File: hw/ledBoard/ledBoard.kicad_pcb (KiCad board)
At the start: 4 copper layers, 34.2 x 34.3 mm, 35 parts, among them J1 Conn_01x13_Socket, J2 Conn_01x13_Socket, J6 726386-2, J7 726386-2, Q1 NMOS, Q2 NMOS, U4 LM5148RGYR

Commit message: hw - ledBoard
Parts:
- removed C21: 470nF, Capacitor_SMD:C_0805_2012Metric_Pad1.18x1.45mm_HandSolder
- removed C22, C23: 100nF, Capacitor_SMD:C_0805_2012Metric_Pad1.18x1.45mm_HandSolder
- removed C24: 4.7uF, Capacitor_SMD:C_0805_2012Metric_Pad1.18x1.45mm_HandSolder
- removed C25: 22p, Capacitor_SMD:C_0805_2012Metric_Pad1.18x1.45mm_HandSolder
- removed C26: 10uF, Capacitor_SMD:C_1210_3225Metric_Pad1.33x2.70mm_HandSolder
- removed C27: 2.7nF, Capacitor_SMD:C_0805_2012Metric_Pad1.18x1.45mm_HandSolder
- removed J7: 726386-2, FASTON:726386-2
- removed NT2: NetTie_2, NetTie:NetTie-2_SMD_Pad0.5mm
- removed Q1, Q2: NMOS, NMOS-CSD18514:DQJ0008A
- removed Rt1: 35.7k, Resistor_SMD:R_0805_2012Metric_Pad1.20x1.40mm_HandSolder
- removed U4: LM5148RGYR, LM5148:VQFN24_RGY_TEX
- added C1: 470nF, Capacitor_SMD:C_0805_2012Metric_Pad1.18x1.45mm_HandSolder, F.Cu at (206.6, 85.8)
- added C19: 0.01uF, Capacitor_SMD:C_0805_2012Metric_Pad1.18x1.45mm_HandSolder, F.Cu at (227.3, 78.4)
- added C2: 10uF, Capacitor_SMD:C_1210_3225Metric_Pad1.33x2.70mm_HandSolder, F.Cu at (214.5, 94.3)
- added C20: 0.01uF, Capacitor_SMD:C_0805_2012Metric_Pad1.18x1.45mm_HandSolder, F.Cu at (228.2, 74.5)
- added C3: 10uF, Capacitor_SMD:C_1210_3225Metric_Pad1.33x2.70mm_HandSolder, F.Cu at (214.5, 91.0)
- added C4: 0.01uF, Capacitor_SMD:C_0805_2012Metric_Pad1.18x1.45mm_HandSolder, F.Cu at (220.9, 90.9)
- added C5: 0.01uF, Capacitor_SMD:C_0805_2012Metric_Pad1.18x1.45mm_HandSolder, F.Cu at (220.9, 95.0)
- added C6: C, Capacitor_SMD:C_0805_2012Metric_Pad1.18x1.45mm_HandSolder, F.Cu at (201.4, 89.3)
- added C7: C, Capacitor_SMD:C_0805_2012Metric_Pad1.18x1.45mm_HandSolder, F.Cu at (204.5, 88.4)
- added C8: 47uF, Capacitor_SMD:C_1210_3225Metric_Pad1.33x2.70mm_HandSolder, B.Cu at (224.2, 83.4)
- added C9: 47uF, Capacitor_SMD:C_1210_3225Metric_Pad1.33x2.70mm_HandSolder, B.Cu at (219.1, 83.4)
- added D2: D, Diode_SMD:D_SOD-523, F.Cu at (200.7, 92.3)
- added D3: STPS3L40UF, STPS3L40:SODFL5436X110N, F.Cu at (211.5, 84.6)
- added D4: D, Diode_SMD:D_SOD-523, B.Cu at (203.1, 81.2)
- added G***: LOGO, LOGO, B.Cu at (209.1, 89.1)
- added IC1: L7986A, LS9B6A:SOIC127P600X170-9N, F.Cu at (209.2, 91.6)
- added IC2: L7986A, LS9B6A:SOIC127P600X170-9N, F.Cu at (205.7, 81.0)
- added J3: Conn_01x02, Connector_JST:JST_XH_B2B-XH-A_1x02_P2.50mm_Vertical, F.Cu at (230.0, 86.7)
- added J5: Conn_01x03_Socket, Connector_PinSocket_2.54mm:PinSocket_1x03_P2.54mm_Vertical, B.Cu at (231.1, 75.1)
- added J8: Conn_01x05_Socket, Connector_PinSocket_2.54mm:PinSocket_1x05_P2.54mm_Vertical, B.Cu at (233.7, 70.0)
- added J9: Conn_01x03_Socket, Connector_PinSocket_2.54mm:PinSocket_1x03_P2.54mm_Vertical, B.Cu at (218.4, 90.3)
- added L2: L, Inductor_SMD:L_Bourns-SRN8040_8x8.15mm, F.Cu at (214.1, 72.5)
- added R10: R, Resistor_SMD:R_0805_2012Metric_Pad1.20x1.40mm_HandSolder, B.Cu at (209.2, 78.5)
- added R11: R, Resistor_SMD:R_0805_2012Metric_Pad1.20x1.40mm_HandSolder, B.Cu at (203.3, 84.3)
- added R12: 10m, Resistor_SMD:R_0815_2038Metric_Pad1.20x4.05mm_HandSolder, F.Cu at (220.7, 74.3)
- added R2: R, Resistor_SMD:R_0805_2012Metric_Pad1.20x1.40mm_HandSolder, F.Cu at (204.5, 96.3)
- added U1: INA180A4, Package_TO_SOT_SMD:SOT-23-5, F.Cu at (227.2, 81.2)
- added U2: INA180A4, Package_TO_SOT_SMD:SOT-23-5, F.Cu at (227.7, 70.6)
- C10, C11, C16, C17: moved to B.Cu
- C12: value 0.01uF -> 470nF
- C13, C14: value 0.01uF -> C; moved to B.Cu
- C15: value 10uF -> 47uF; moved to B.Cu
- C18: value 0.01uF -> 47uF; footprint Capacitor_SMD:C_0805_2012Metric_Pad1.18x1.45mm_HandSolder -> Capacitor_SMD:C_1210_3225Metric_Pad1.33x2.70mm_HandSolder; moved to B.Cu
- D1: value 1N4448 -> STPS3L40UF; footprint Diode_SMD:D_SOD-523 -> STPS3L40:SODFL5436X110N
- J1: value Conn_01x13_Socket -> Conn_02x11_Socket; footprint Connector_PinSocket_2.54mm:PinSocket_1x13_P2.54mm_Vertical -> Library:LedBoardPinHeader
- J2: value Conn_01x13_Socket -> Conn_01x02; footprint Connector_PinSocket_2.54mm:PinSocket_1x13_P2.54mm_Vertical -> Connector_JST:JST_XH_B2B-XH-A_1x02_P2.50mm_Vertical
- J6: value 726386-2 -> Conn_01x03_Socket; footprint FASTON:726386-2 -> Connector_PinSocket_2.54mm:PinSocket_1x03_P2.54mm_Vertical; moved to B.Cu
- L1: value 3.6uH -> L
- R1: value 22.5k -> R
- R3: value 10m -> R; footprint Resistor_SMD:R_0815_2038Metric_Pad1.20x4.05mm_HandSolder -> Resistor_SMD:R_0805_2012Metric_Pad1.20x1.40mm_HandSolder
- R4: value 41.2k -> R; moved to F.Cu
- R5: value 10k -> 100k; moved to F.Cu
- R6: value 100k -> 10m; footprint Resistor_SMD:R_0805_2012Metric_Pad1.20x1.40mm_HandSolder -> Resistor_SMD:R_0815_2038Metric_Pad1.20x4.05mm_HandSolder
- R7: value 10k -> R; moved to B.Cu
- R8: value 140k -> 100k; moved to B.Cu
- R9: value 10k -> R
- moved R6 58.6 mm to (224.4, 86.1), turned to 180 degrees
- moved D1 58.5 mm to (207.5, 73.5), turned to 90 degrees
- moved C11 55.6 mm to (224.2, 86.7), turned to 0 degrees
- moved J6 53.9 mm to (223.5, 90.3), turned to 180 degrees
- moved C10 47.5 mm to (219.1, 86.7), turned to 180 degrees
- moved C15 45.0 mm to (215.2, 70.0)
- moved J2 40.6 mm to (230.0, 93.6)
- moved L1 39.3 mm to (218.1, 84.1), turned to 180 degrees
- moved J1 38.1 mm to (203.2, 70.0)
- moved C18 36.7 mm to (221.1, 69.8)
- moved C17 35.6 mm to (221.1, 75.1), turned to 0 degrees
- moved R9 35.1 mm to (213.0, 78.5)
- moved R3 30.6 mm to (204.5, 90.4), turned to 180 degrees
- moved C16 26.5 mm to (215.2, 75.0), turned to 180 degrees
- moved C12 23.3 mm to (210.1, 96.3), turned to 180 degrees
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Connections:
- C10 pad 1: /LED_OUT -> Net-(U1-+)
- C11 pad 1: /LED_OUT -> Net-(U1-+)
- C13 pad 1: /24V -> Net-(IC2-COMP)
- C13 pad 2: GND -> Net-(IC2-FB)
- C14 pad 1: /24V -> Net-(IC2-COMP)
- C14 pad 2: GND -> Net-(C14-Pad2)
- C15 pad 1: /24V -> Net-(U2-+)
- C16 pad 1: /LED_OUT -> Net-(U2-+)
- C17 pad 1: /LED_OUT -> Net-(U2-+)
- C18 pad 1: /24V -> Net-(U2-+)
- D1 pad 2: /RA2 -> GND
- J1 pad 1: /5.2V -> GND
- J1 pad 10: /RA4 -> /RA1
- J1 pad 12: /RA6 -> /RA2
- J1 pad 2: /5.2V -> GND
- J1 pad 3: GND -> /5.2V
- J1 pad 4: /VDD -> /5.2V
- J1 pad 6: /RA0 -> /VDD
- J1 pad 8: /RA2 -> /RA0
- J2 pad 1: /~{MCLR} -> /LED_OUT_0
- J2 pad 2: /VDD -> GND
- J6 pad 1: /24V -> GND
- J6 pad 2: /24V -> GND
- L1 pad 1: /ISNS+ -> Net-(U1-+)
- R1 pad 1: Net-(U4A-FB) -> Net-(U1-+)
- R1 pad 2: Net-(D1-K) -> Net-(IC1-FB)
- R3 pad 1: /LED_OUT -> Net-(IC1-FB)
- R3 pad 2: /ISNS+ -> Net-(C6-Pad2)
- R4 pad 1: GNDA -> Net-(IC1-FB)
- R5 pad 1: Net-(U4A-EXTCOMP) -> /RA2
- R5 pad 2: Net-(C27-Pad1) -> GND
- R6 pad 1: /VDD -> /LED_OUT_0
- R6 pad 2: /RA0 -> Net-(U1-+)
- R7 pad 1: Net-(U4A-FB) -> Net-(IC2-FB)
- R7 pad 2: GNDA -> Net-(C14-Pad2)
- R8 pad 1: /LED_OUT -> /RA0
- R8 pad 2: Net-(U4A-FB) -> GND
- R9 pad 1: /VDDA -> Net-(U2-+)
- R9 pad 2: Net-(U4A-EXTCOMP) -> Net-(IC2-FB)
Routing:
- net GND: track 67.5 -> 107.6 mm, vias 36 -> 54
- net Net-(U1-+): track 0.00 -> 27.1 mm, vias 0 -> 9
- net /24V: track 5.99 -> 31.7 mm, vias 12 -> 10
- net /RA2: track 0.00 -> 21.9 mm, vias 0 -> 2
- net Net-(IC2-FB): track 0.00 -> 20.7 mm, vias 0 -> 1
- net /LED_OUT: track 17.2 -> 0.00 mm, vias 3 -> 0
- net /LED_OUT_0: track 0.00 -> 16.6 mm
- net Net-(U2-+): track 0.00 -> 15.1 mm, vias 0 -> 8
- net /ISNS+: track 12.7 -> 0.00 mm, vias 2 -> 0
- net Net-(IC1-FB): track 0.00 -> 9.69 mm
- net /VDD: track 0.00 -> 9.54 mm, vias 0 -> 4
- net Net-(IC2-COMP): track 0.00 -> 8.42 mm, vias 0 -> 1
- net /RB1: track 0.00 -> 8.01 mm, vias 0 -> 1
- net /RA0: track 0.00 -> 7.83 mm, vias 0 -> 1
- net Net-(D1-K): track 0.00 -> 7.81 mm
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- added copper zone on F.Cu, net /LED_OUT_0
- added copper zone on F.Cu, net /LED_OUT_1
- added copper zone on In2.Cu, net /LED_OUT_1
- added copper zone on In2.Cu, net /VDD
- added copper zone on In1.Cu, net GND
- added copper zone on In2.Cu, net GND
- added copper zone on F.Cu, net Net-(D1-K)
- added copper zone on B.Cu, net Net-(U1-+)
- added copper zone on F.Cu, net Net-(U1-+)
- added copper zone on B.Cu, net Net-(U2-+)
- added copper zone on F.Cu, net Net-(U2-+)
- removed copper zone on F.Cu, net /ISNS+
- removed copper zone on F.Cu, net /LED_OUT
- removed copper zone on F.Cu, net GNDA
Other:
- board size 34.2 x 34.3 mm -> 37 x 29.7 mm
- board text added: "+24V"
- board text added: "2024 Jakub Charvot, FEKT VUT"
- board text added: "3.3V"
- board text added: "5.2V"
- board text added: "GND"
- board text added: "ICSP"
- board text added: "JLCJLCJLCJLC"
- board text added: "RA0"
- board text added: "RA1"
- board text added: "RA2"
- board text added: "RA3"
- board text added: "RB0"
- board text added: "RB1"
- board text added: "RB5"

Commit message: hw - ledboard, compensation
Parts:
- added C21: C, Capacitor_SMD:C_0805_2012Metric_Pad1.18x1.45mm_HandSolder, B.Cu at (216.8, 78.5)
- added C22: C, Capacitor_SMD:C_0805_2012Metric_Pad1.18x1.45mm_HandSolder, B.Cu at (205.4, 91.3)
- added R13: R, Resistor_SMD:R_0805_2012Metric_Pad1.20x1.40mm_HandSolder, B.Cu at (215.0, 80.5)
- added R14: R, Resistor_SMD:R_0805_2012Metric_Pad1.20x1.40mm_HandSolder, B.Cu at (203.5, 93.3)
- R1, R9: value R -> 190k
- R10, R2: value R -> 10k
- R11, R4: value R -> 127k
- moved G*** 2.38 mm to (211.1, 87.7), turned to -60 degrees
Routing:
- net Net-(IC2-FB): track 20.7 -> 23.6 mm
- net Net-(C21-Pad2): track 0.00 -> 2.78 mm
- net Net-(IC1-FB): track 9.69 -> 11.7 mm, vias 0 -> 1
- net Net-(C22-Pad2): track 0.00 -> 1.94 mm
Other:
- board text added: "v 1.0"

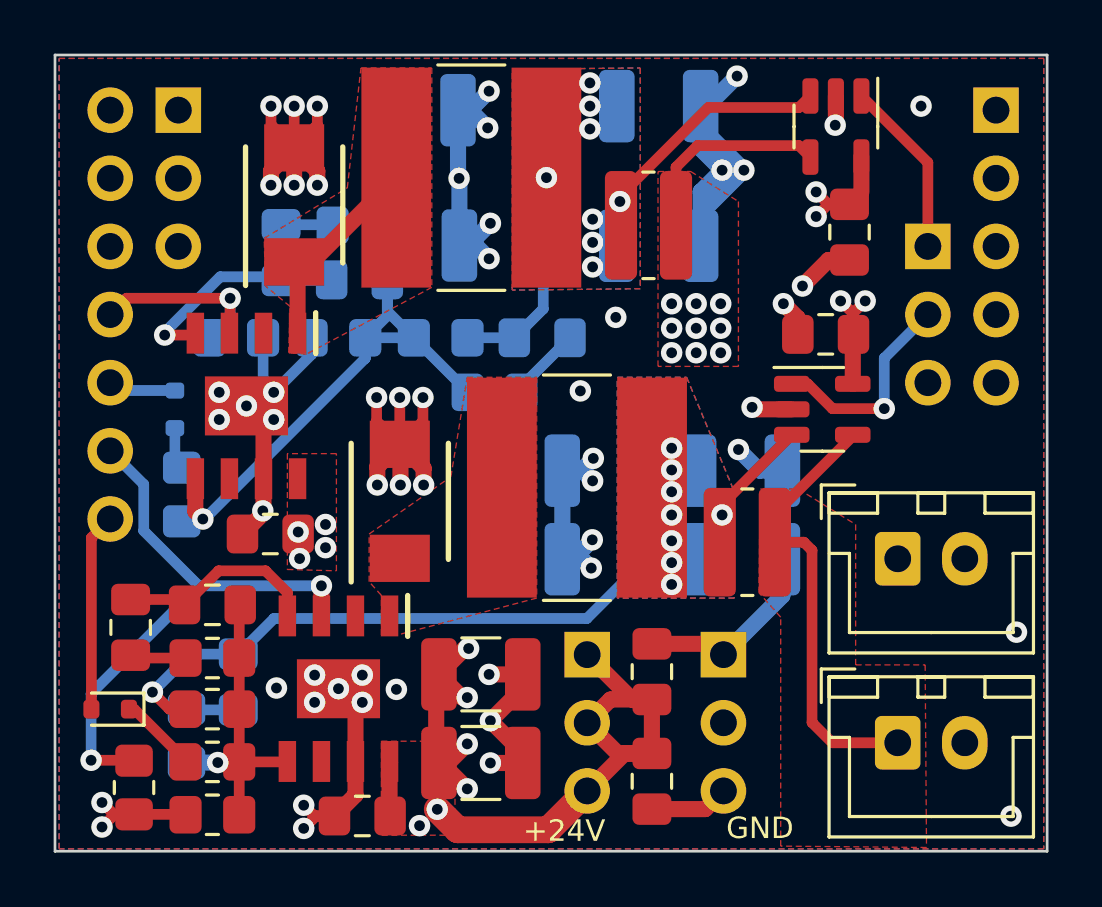
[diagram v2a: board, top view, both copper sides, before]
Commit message: hw - led board redesign
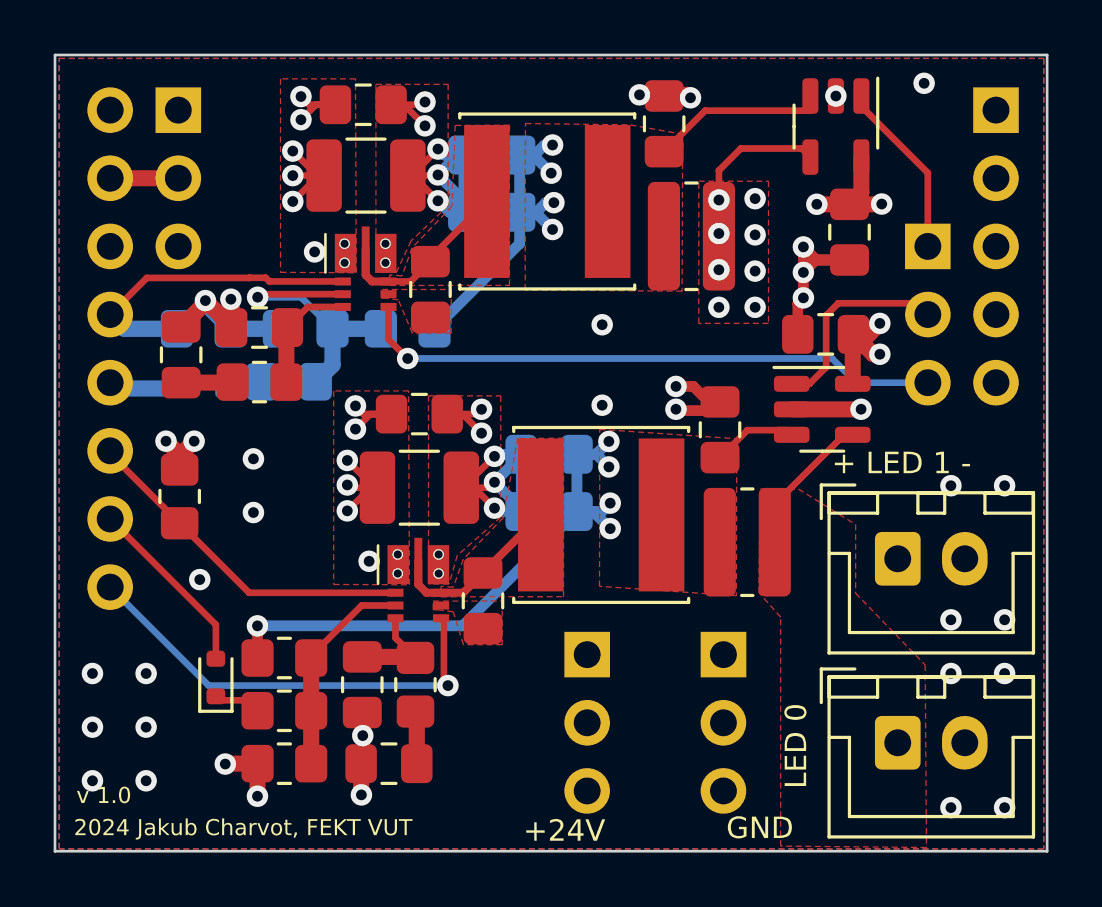
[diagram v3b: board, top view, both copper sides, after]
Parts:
- removed C1, C12: 470nF, Capacitor_SMD:C_0805_2012Metric_Pad1.18x1.45mm_HandSolder
- removed C11, C18: 47uF, Capacitor_SMD:C_1210_3225Metric_Pad1.33x2.70mm_HandSolder
- removed C21, C22: C, Capacitor_SMD:C_0805_2012Metric_Pad1.18x1.45mm_HandSolder
- removed D1, D3: STPS3L40UF, STPS3L40:SODFL5436X110N
- removed IC1, IC2: L7986A, LS9B6A:SOIC127P600X170-9N
- removed R13, R14: R, Resistor_SMD:R_0805_2012Metric_Pad1.20x1.40mm_HandSolder
- added C23: 100nF, Capacitor_SMD:C_0805_2012Metric_Pad1.18x1.45mm_HandSolder, F.Cu at (212.6, 76.7)
- added C24: 100nF, Capacitor_SMD:C_0805_2012Metric_Pad1.18x1.45mm_HandSolder, F.Cu at (214.6, 88.3)
- added U3: AP63356Q, Library:V-DFN3020-13, F.Cu at (211.0, 86.2)
- added U4: AP63356Q, Library:V-DFN3020-13, F.Cu at (209.0, 74.6)
- C10, C16, C17, C9: value 47uF -> 22uF; footprint Capacitor_SMD:C_1210_3225Metric_Pad1.33x2.70mm_HandSolder -> Capacitor_SMD:C_0805_2012Metric_Pad1.18x1.45mm_HandSolder
- C13: value C -> 100nF; moved to F.Cu
- C14: value C -> 6.8nF; moved to F.Cu
- C15, C8: value 47uF -> 22uF; footprint Capacitor_SMD:C_1210_3225Metric_Pad1.33x2.70mm_HandSolder -> Capacitor_SMD:C_0805_2012Metric_Pad1.18x1.45mm_HandSolder; moved to F.Cu
- C19, C20: value 0.01uF -> 100nF
- C4, C5: value 0.01uF -> 10nF
- C6: value C -> 6.8nF
- C7: value C -> 100nF
- D2, D4: value D -> RB501SM
- L1, L2: value L -> 10uH; footprint Inductor_SMD:L_Bourns-SRN8040_8x8.15mm -> Inductor_SMD:L_Changjiang_FNR6045S
- R1, R9: value 190k -> 140k
- R11, R4: value 127k -> 100k
- R3: value R -> 47k
- R7: value R -> 47k; moved to F.Cu
- moved C5 27.4 mm to (210.1, 69.8), turned to 0 degrees
- moved C3 19.1 mm to (210.2, 72.4)
- moved C4 12.9 mm to (212.2, 81.3), turned to 0 degrees
- moved R5 11.0 mm to (203.2, 84.4), turned to 90 degrees
- moved C6 10.9 mm to (211.1, 94.4), turned to 0 degrees
- moved C2 10.5 mm to (212.2, 84.1)
- moved R3 7.63 mm to (212.0, 91.4), turned to -90 degrees
- moved R7 6.93 mm to (206.2, 80.1)
- moved C17 6.35 mm to (214.9, 73.8), turned to 180 degrees
- moved C7 6.33 mm to (210.1, 91.4), turned to 90 degrees
- moved C15 6.14 mm to (221.3, 70.5), turned to 90 degrees
- moved R11 5.80 mm to (207.3, 80.1), turned to 180 degrees
- moved C14 5.33 mm to (203.3, 79.1), turned to -90 degrees
- moved C10 4.42 mm to (217.0, 82.8)
- moved C13 4.13 mm to (206.2, 78.1)
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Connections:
- C13 pad 1: Net-(IC2-COMP) -> GND
- C13 pad 2: Net-(IC2-FB) -> Net-(U4-COMP)
- C14 pad 1: Net-(IC2-COMP) -> GND
- C6 pad 1: Net-(IC1-COMP) -> GND
- C7 pad 1: Net-(IC1-COMP) -> GND
- C7 pad 2: Net-(IC1-FB) -> Net-(U3-COMP)
- R1 pad 2: Net-(IC1-FB) -> Net-(U3-FB)
- R10 pad 1: Net-(IC2-FB) -> Net-(U4-FB)
- R11 pad 1: Net-(IC2-FB) -> Net-(U4-FB)
- R2 pad 1: Net-(IC1-FB) -> Net-(U3-FB)
- R3 pad 1: Net-(IC1-FB) -> Net-(U3-COMP)
- R4 pad 1: Net-(IC1-FB) -> Net-(U3-FB)
- R7 pad 1: Net-(IC2-FB) -> Net-(U4-COMP)
- R9 pad 2: Net-(IC2-FB) -> Net-(U4-FB)
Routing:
- net GND: track 107.6 -> 61.3 mm, vias 54 -> 51
- net Net-(IC2-FB): track 23.6 -> 0.00 mm, vias 1 -> 0
- net /RB5: track 0.00 -> 22.0 mm, vias 0 -> 1
- net /24V: track 31.7 -> 14.4 mm, vias 10 -> 16
- net /RA4: track 0.00 -> 16.7 mm, vias 0 -> 1
- net Net-(IC1-FB): track 11.7 -> 0.00 mm, vias 1 -> 0
- net /LED_OUT_0: track 16.6 -> 5.40 mm
- net Net-(U4-FB): track 0.00 -> 10.5 mm, vias 0 -> 1
- net /RA2: track 21.9 -> 12.9 mm, vias 2 -> 0
- net Net-(IC2-COMP): track 8.42 -> 0.00 mm, vias 1 -> 0
- net Net-(U3-FB): track 0.00 -> 7.94 mm
- net Net-(IC1-COMP): track 7.71 -> 0.00 mm
- net Net-(U3-SW): track 0.00 -> 6.78 mm
- net Net-(U2-+): track 15.4 -> 20.2 mm, vias 8 -> 4
- net Net-(U4-COMP): track 0.00 -> 4.44 mm
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- added copper zone on F.Cu, net Net-(U3-BST)
- added copper zone on F.Cu, net Net-(U4-BST)
- removed copper zone on B.Cu, net Net-(U1-+)
- removed copper zone on B.Cu, net Net-(U2-+)
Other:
- board text added: "+ LED 1 -"
- board text added: "LED 0"
- board text added: "RA4"
